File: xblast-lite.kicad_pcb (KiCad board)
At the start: 2 copper layers, 70 x 36 mm, 30 parts, among them J1 TC2050, J2 XBOX LPC, J3 GPIO, J4 LCD, J5 PLCC-32 Socket, Q1 BC846, Q2 BC846, U1 74LVC125, U3 XC9572XL-xxVQx44, U4 TPS27081A

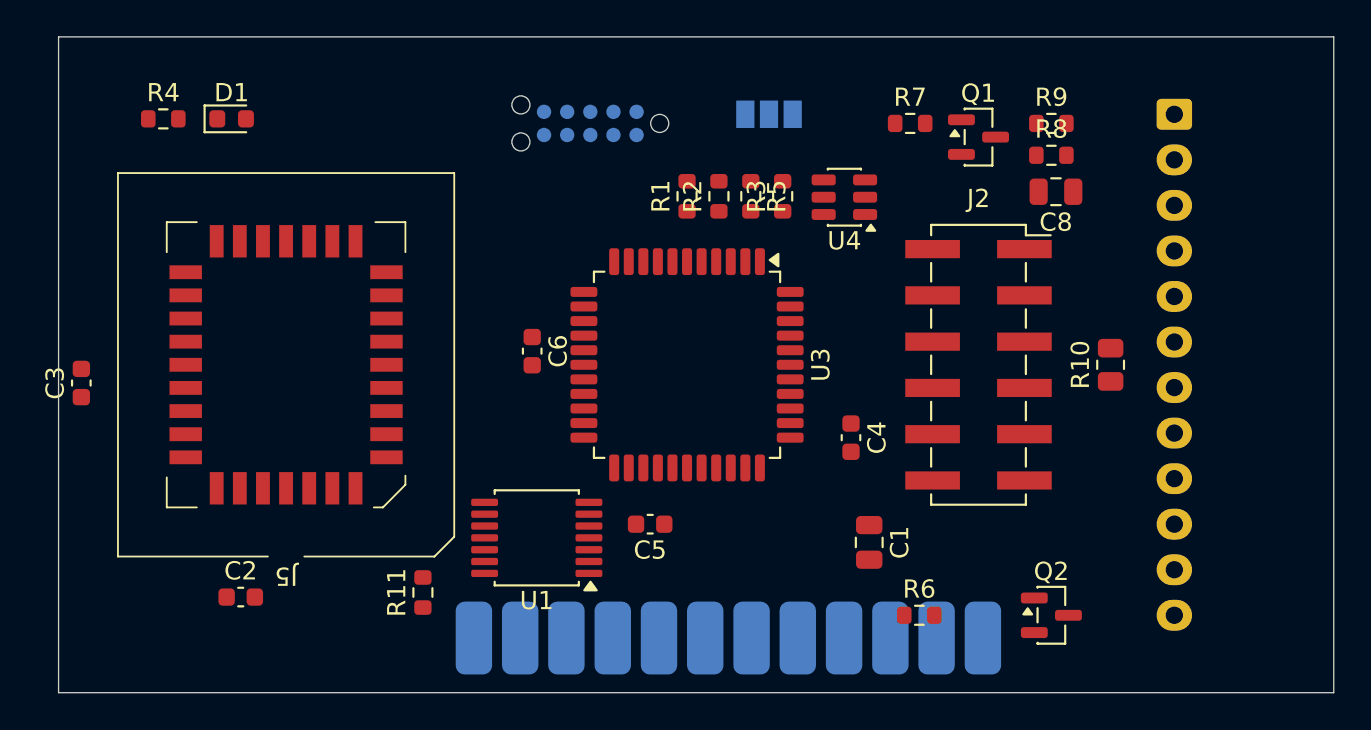
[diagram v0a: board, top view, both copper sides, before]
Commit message: Finished routing, need to fix silkscreen
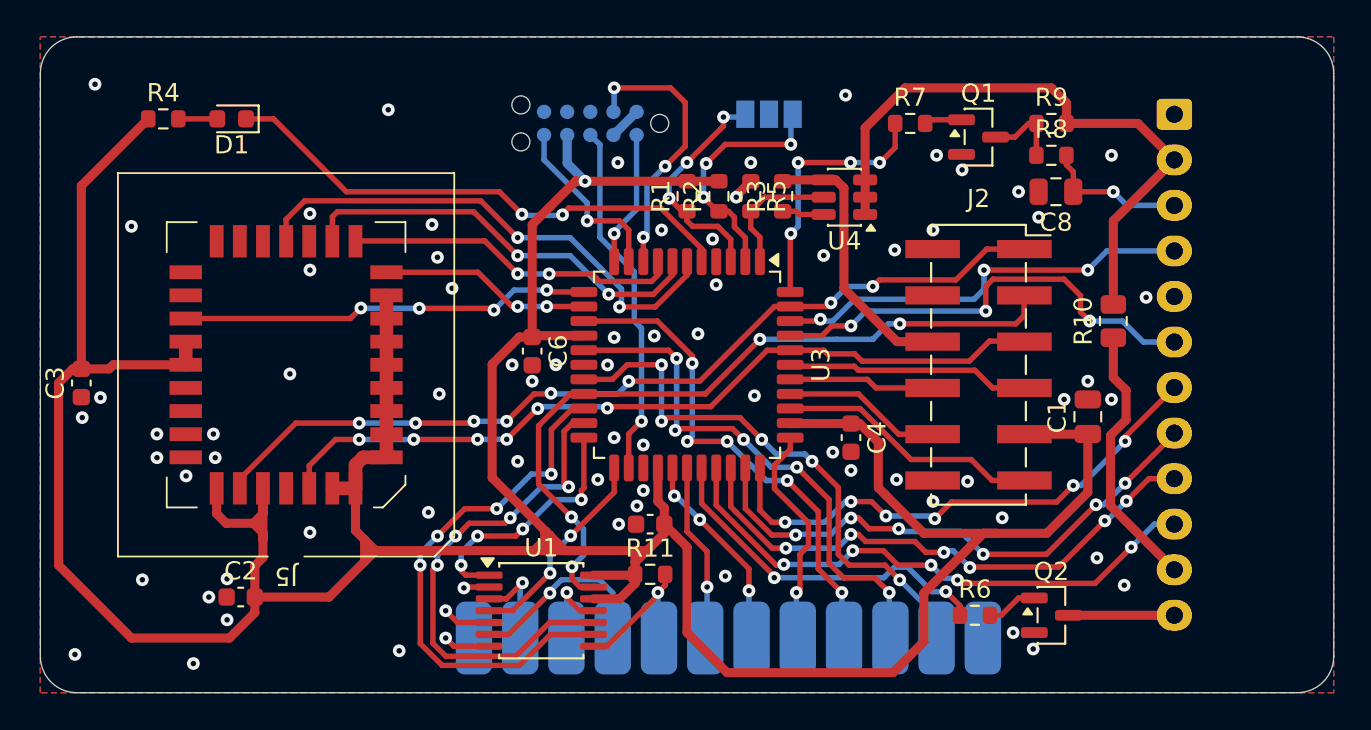
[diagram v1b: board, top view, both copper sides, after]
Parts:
- moved C1 13.8 mm to (166.5, 90.8), turned to 90 degrees
- moved R11 12.5 mm to (142.5, 99.5), turned to 0 degrees
- moved U1 4.01 mm to (136.5, 101.5), turned to 0 degrees
- moved R6 3.05 mm to (160.3, 101.8)
- moved R10 2.40 mm to (167.9, 85.6)
- turned D1 to 180 degrees
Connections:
- net Net-(J4-Pin_11) renamed /LCD_BL_V
- net Net-(Q2-B) renamed /LCD_BL_I
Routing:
- net +3V3: track 0.00 -> 213.1 mm, vias 0 -> 1
- net /XLCLK: track 0.00 -> 48.9 mm, vias 0 -> 8
- net /~{XLRESET}: track 0.00 -> 43.9 mm, vias 0 -> 6
- net /~{XLFRAME}: track 0.00 -> 41.3 mm, vias 0 -> 4
- net +5V: track 0.00 -> 34.3 mm
- net /GPI0: track 0.00 -> 32.0 mm, vias 0 -> 5
- net /LCD_D7: track 0.00 -> 31.0 mm, vias 0 -> 5
- net /LCD_D6: track 0.00 -> 30.9 mm, vias 0 -> 6
- net /LCD_D5: track 0.00 -> 30.4 mm, vias 0 -> 6
- net /A19_VAL: track 0.00 -> 29.4 mm, vias 0 -> 4
- net /GPI1: track 0.00 -> 29.4 mm, vias 0 -> 5
- net /LCD_D4: track 0.00 -> 29.3 mm, vias 0 -> 6
- net /LED: track 0.00 -> 29.0 mm, vias 0 -> 2
- net /FLAD3: track 0.00 -> 28.2 mm, vias 0 -> 2
- net /A19_CTRL: track 0.00 -> 28.0 mm, vias 0 -> 4
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- added copper zone on B.Cu, net GND
- added copper zone on F.Cu, net GND
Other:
- board size 70 x 36 mm -> 71 x 36 mm

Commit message: Finished layout
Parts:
- J1: value TC2050 -> JTAG
- moved R10 7.07 mm to (174.9, 86.6)
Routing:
- net /LCD_BL_V: track 14.8 -> 13.2 mm
- net +5V: track 34.3 -> 35.4 mm
- net /LCD_E: track 25.1 -> 24.6 mm, vias 3 -> 2
- net /LCD_D5: vias 6 -> 4
- net /LCD_D6: vias 6 -> 4
- net /LCD_SW_CT: vias 1 -> 0
- net GND: vias 74 -> 85
- net /LCD_RS: vias 3 -> 2
- net /LCD_D7: vias 5 -> 4
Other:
- board text added: "512.256"
- board text added: "A"
- board text added: "A15"
- board text added: "A19"
- board text added: "D0"
- board text added: "D4"
- board text added: "D5"
- board text added: "D6"
- board text added: "D7"
- board text added: "E"
- board text added: "GND"
- board text added: "GPI0"
- board text added: "GPI1"
- board text added: "GPO0"
- board text added: "GPO1"
- board text added: "GPO2"
- board text added: "GPO3"
- board text added: "K"
- board text added: "L1"
- board text added: "RS"
- board text added: "RW"
- board text added: "V0"
- board text added: "VDD"
- board text added: "VSS"

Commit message: Minor changes
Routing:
- net /FLAD2: track 23.2 -> 24.7 mm
- net /FLAD3: track 28.2 -> 29.2 mm
- net /LCD_E: track 24.6 -> 24.0 mm
- net GND: vias 85 -> 88
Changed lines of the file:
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@@
 			(at 13.55 5.15 90)
 			(layer "B.SilkS")
+			(hide yes)
 			(effects
 				(font
@@
 	)
 	(via
+		(at 140.8 78.7)
+		(size 0.6)
+		(drill 0.3)
+		(layers "F.Cu" "B.Cu")
+		(free yes)
+		(net "GND")
+	)
+	(via
 		(at 167.8 89.9)
 		(size 0.7)
@@
 	)
 	(via
+		(at 136.7 78.5)
+		(size 0.6)
+		(drill 0.3)
+		(layers "F.Cu" "B.Cu")
+		(free yes)
+		(net "GND")
+	)
+	(via
 		(at 140.5 92)
 		(size 0.7)
@@
 	)
 	(via
+		(at 137.6 82)
+		(size 0.6)
+		(drill 0.3)
+		(layers "F.Cu" "B.Cu")
+		(free yes)
+		(net "GND")
+	)
+	(via
 		(at 131.6 83.8)
 		(size 0.7)
@@
 	)
 	(segment
-		(start 138.085051 82.010051)
-		(end 135.200001 82.010051)
+		(start 140.2 83.007106)
+		(end 138.15858 80.965686)
 		(width 0.3)
 		(layer "B.Cu")
@@
 	(segment
 		(start 140.2 84.125)
-		(end 138.085051 82.010051)
+		(end 140.2 83.007106)
+		(width 0.3)
+		(layer "B.Cu")
+		(net "/FLAD2")
+	)
+	(segment
+		(start 138.15858 80.965686)
+		(end 136.244366 80.965686)
+		(width 0.3)
+		(layer "B.Cu")
+		(net "/FLAD2")
+	)
+	(segment
+		(start 136.244366 80.965686)
+		(end 135.200001 82.010051)
 		(width 0.3)
 		(layer "B.Cu")
@@
 	)
 	(segment
-		(start 138.085051 81.020101)
+		(start 138.365686 80.465686)
+		(end 135.754416 80.465686)
+		(width 0.3)
+		(layer "B.Cu")
+		(net "/FLAD3")
+	)
+	(segment
+		(start 135.754416 80.465686)
 		(end 135.200001 81.020101)
 		(width 0.3)
@@
 	)
 	(segment
-		(start 140.9 83.83505)
-		(end 138.085051 81.020101)
+		(start 140.9 84.715563)
+		(end 140.9 83)
 		(width 0.3)
 		(layer "B.Cu")
@@
 	)
 	(segment
-		(start 140.9 84.715563)
-		(end 140.9 83.83505)
+		(start 140.9 83)
+		(end 138.365686 80.465686)
 		(width 0.3)
 		(layer "B.Cu")
@@
 	)
 	(segment
-		(start 150.1625 86.4)
-		(end 151.91005 86.4)
+		(start 160.9 83.7)
+		(end 161.3 83.3)
+		(width 0.3)
+		(layer "F.Cu")
+		(net "/LCD_E")
+	)
+	(segment
+		(start 155.412026 85.051366)
+		(end 159.948634 85.051366)
 		(width 0.3)
 		(layer "F.Cu")
@@
 	)
 	(segment
-		(start 161.28995 83.3)
-		(end 160.9 83.68995)
+		(start 165.2 83.3)
+		(end 168.65 86.75)
 		(width 0.3)
 		(layer "F.Cu")
@@
 	)
 	(segment
-		(start 160.9 83.68995)
-		(end 160.9 85.051366)
+		(start 150.1625 86.4)
+		(end 152.965686 86.4)
 		(width 0.3)
 		(layer "F.Cu")
@@
 	)
 	(segment
-		(start 165.2 83.3)
-		(end 168.65 86.75)
+		(start 155.41066 85.05)
+		(end 155.412026 85.051366)
 		(width 0.3)
 		(layer "F.Cu")
@@
 	)
 	(segment
-		(start 151.91005 86.4)
-		(end 152.444364 85.865686)
+		(start 159.948634 85.051366)
+		(end 160.9 84.1)
 		(width 0.3)
 		(layer "F.Cu")
@@
 	)
 	(segment
-		(start 165.2 83.3)
-		(end 161.28995 83.3)
+		(start 152.965686 86.4)
+		(end 153.5 85.865686)
 		(width 0.3)
 		(layer "F.Cu")
@@
 	)
 	(segment
-		(start 152.444364 85.865686)
-		(end 153.5 85.865686)
+		(start 160.9 84.1)
+		(end 160.9 83.7)
+		(width 0.3)
+		(layer "F.Cu")
+		(net "/LCD_E")
+	)
+	(segment
+		(start 161.3 83.3)
+		(end 165.2 83.3)
 		(width 0.3)
 		(layer "F.Cu")
@@
 	)
 	(via
-		(at 160.9 85.051366)
+		(at 153.5 85.865686)
 		(size 0.7)
 		(drill 0.3)
@@
 	)
 	(via
-		(at 153.5 85.865686)
-		(size 0.7)
+		(at 155.41066 85.05)
+		(size 0.6)
 		(drill 0.3)
 		(layers "F.Cu" "B.Cu")
@@
 	)
 	(segment
+		(start 155.409294 85.051366)
+		(end 154.31432 85.051366)
+		(width 0.3)
+		(layer "B.Cu")
+		(net "/LCD_E")
+	)
+	(segment
 		(start 154.31432 85.051366)
-		(end 160.9 85.051366)
+		(end 153.5 85.865686)
 		(width 0.3)
 		(layer "B.Cu")
@@
 	)
 	(segment
-		(start 153.5 85.865686)
-		(end 154.31432 85.051366)
+		(start 155.41066 85.05)
+		(end 155.409294 85.051366)
 		(width 0.3)
 		(layer "B.Cu")

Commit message: Cleanup layout
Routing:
- net +3V3: track 213.1 -> 265.2 mm
- net /~{XLRESET}: track 43.9 -> 48.6 mm, vias 6 -> 4
- net /FLAD3: track 29.2 -> 25.7 mm, vias 2 -> 0
- net /LCD_D5: track 30.4 -> 27.2 mm
- net /LCD_D6: track 30.9 -> 27.7 mm
- net GND: track 9.64 -> 6.64 mm, vias 88 -> 75
- net /FLAD2: track 24.7 -> 21.8 mm, vias 2 -> 0
- net /LCD_D7: track 31.0 -> 28.2 mm
- net /GPI1: track 29.4 -> 31.9 mm, vias 5 -> 3
- net /GPI0: track 32.0 -> 34.6 mm, vias 5 -> 3
- net /FLAD0: track 11.6 -> 14.1 mm, vias 2 -> 0
- net /XLCLK: track 48.9 -> 51.2 mm, vias 8 -> 6
- net /~{XLFRAME}: track 41.3 -> 43.6 mm
- net /TDI: track 15.3 -> 13.0 mm
- net /LCD_D4: track 29.5 -> 27.5 mm, vias 6 -> 4
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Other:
- board text added: "XBLAST LITE v1 Designed by Clegg"

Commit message: Fix DRC issues
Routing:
- net GND: track 6.64 -> 8.02 mm
- net /D0_VAL: track 14.3 -> 13.6 mm
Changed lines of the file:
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@@
+	)
+	(segment
+		(start 147.5 78.7)
+		(end 147.1 78.7)
+		(width 0.5)
+		(layer "F.Cu")
+		(net "GND")
 	)
 	(segment
@@
 	)
 	(segment
+		(start 148 77.925)
+		(end 148 78.2)
+		(width 0.5)
+		(layer "F.Cu")
+		(net "GND")
+	)
+	(segment
 		(start 132.3 100.2)
 		(end 132.25 100.25)
 		(width 0.3)
+		(layer "F.Cu")
+		(net "GND")
+	)
+	(segment
+		(start 148 78.2)
+		(end 147.5 78.7)
+		(width 0.5)
 		(layer "F.Cu")
 		(net "GND")
@@
 	)
 	(segment
-		(start 132.1 99)
-		(end 132.1 98.3)
-		(width 0.3)
-		(layer "B.Cu")
-		(net "/D0_VAL")
-	)
-	(segment
 		(start 133.6375 100.85)
 		(end 134.58015 100.85)
@@
 	)
 	(segment
+		(start 126.477609 85.143989)
+		(end 126.477609 85.182389)
+		(width 0.2)
+		(layer "F.Cu")
+		(net "/XLCLK")
+	)
+	(segment
 		(start 141.65 84.8)
 		(end 150.1625 84.8)
@@
 	)
 	(segment
+		(start 126.477609 85.182389)
+		(end 119.95 91.709998)
+		(width 0.2)
+		(layer "F.Cu")
+		(net "/XLCLK")
+	)
+	(segment
+		(start 154.096814 83.2)
+		(end 153.9125 83.384314)
+		(width 0.2)
+		(layer "F.Cu")
+		(net "/XLCLK")
+	)
+	(segment
+		(start 159.4 83.2)
+		(end 154.096814 83.2)
+		(width 0.2)
+		(layer "F.Cu")
+		(net "/XLCLK")
+	)
+	(segment
+		(start 140.55 83.7)
+		(end 141.65 84.8)
+		(width 0.2)
+		(layer "F.Cu")
+		(net "/XLCLK")
+	)
+	(segment
+		(start 129.6 84.892567)
+		(end 137.55 84.892567)
+		(width 0.2)
+		(layer "F.Cu")
+		(net "/XLCLK")
+	)
+	(segment
+		(start 160.95 81.65)
+		(end 159.4 83.2)
+		(width 0.2)
+		(layer "F.Cu")
+		(net "/XLCLK")
+	)
+	(segment
 		(start 119.95 91.709998)
 		(end 119.95 94.78)
@@
 	)
 	(segment
-		(start 154.096814 83.2)
-		(end 153.9125 83.384314)
-		(width 0.2)
-		(layer "F.Cu")
-		(net "/XLCLK")
-	)
-	(segment
-		(start 159.4 83.2)
-		(end 154.096814 83.2)
-		(width 0.2)
-		(layer "F.Cu")
-		(net "/XLCLK")
-	)
-	(segment
-		(start 140.55 83.7)
-		(end 141.65 84.8)
-		(width 0.2)
-		(layer "F.Cu")
-		(net "/XLCLK")
-	)
-	(segment
-		(start 160.95 81.65)
-		(end 159.4 83.2)
-		(width 0.2)
-		(layer "F.Cu")
-		(net "/XLCLK")
-	)
-	(segment
 		(start 152.38831 84.152426)
 		(end 151.740736 84.8)
@@
 		(net "/XLCLK")
 	)
-	(segment
-		(start 137.55 84.892567)
-		(end 129.416453 84.892567)
-		(width 0.2)
-		(layer "F.Cu")
-		(net "/XLCLK")
-	)
-	(segment
-		(start 126.559998 85.1)
-		(end 119.95 91.709998)
-		(width 0.2)
-		(layer "F.Cu")
-		(net "/XLCLK")
-	)
-	(segment
-		(start 129.416453 84.892567)
-		(end 129.409533 84.899487)
-		(width 0.2)
-		(layer "F.Cu")
-		(net "/XLCLK")
-	)
-	(via
-		(at 129.409533 84.899487)
+	(via
+		(at 129.6 84.892567)
 		(size 0.7)
 		(drill 0.3)
@@
 	)
 	(via
-		(at 126.559998 85.1)
+		(at 126.477609 85.143989)
 		(size 0.7)
 		(drill 0.3)
@@
 		(drill 0.3)
 		(layers "F.Cu" "B.Cu")
+		(net "/XLCLK")
+	)
+	(segment
+		(start 129.59308 84.899487)
+		(end 129.6 84.892567)
+		(width 0.2)
+		(layer "B.Cu")
+		(net "/XLCLK")
+	)
+	(segment
+		(start 126.477609 85.143989)
+		(end 126.516009 85.143989)
+		(width 0.2)
+		(layer "B.Cu")
 		(net "/XLCLK")
 	)
@@
 	)
 	(segment
-		(start 126.760511 84.899487)
-		(end 126.559998 85.1)
+		(start 126.516009 85.143989)
+		(end 126.760511 84.899487)
 		(width 0.2)
 		(layer "B.Cu")
@@
 	)
 	(segment
-		(start 129.409533 84.899487)
-		(end 126.760511 84.899487)
-		(width 0.2)
-		(layer "B.Cu")
-		(net "/XLCLK")
-	)
-	(segment
 		(start 140.55 83.7)
 		(end 138.7 83.7)
 		(width 0.2)
 		(layer "B.Cu")
+		(net "/XLCLK")
+	)
+	(segment
+		(start 126.760511 84.899487)
+		(end 129.59308 84.899487)
+		(width 0.2)
+		(layer "B.Cu")
